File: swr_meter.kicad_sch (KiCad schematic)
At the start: 15 parts, among them U401 LTC5507, U402 LTC5507

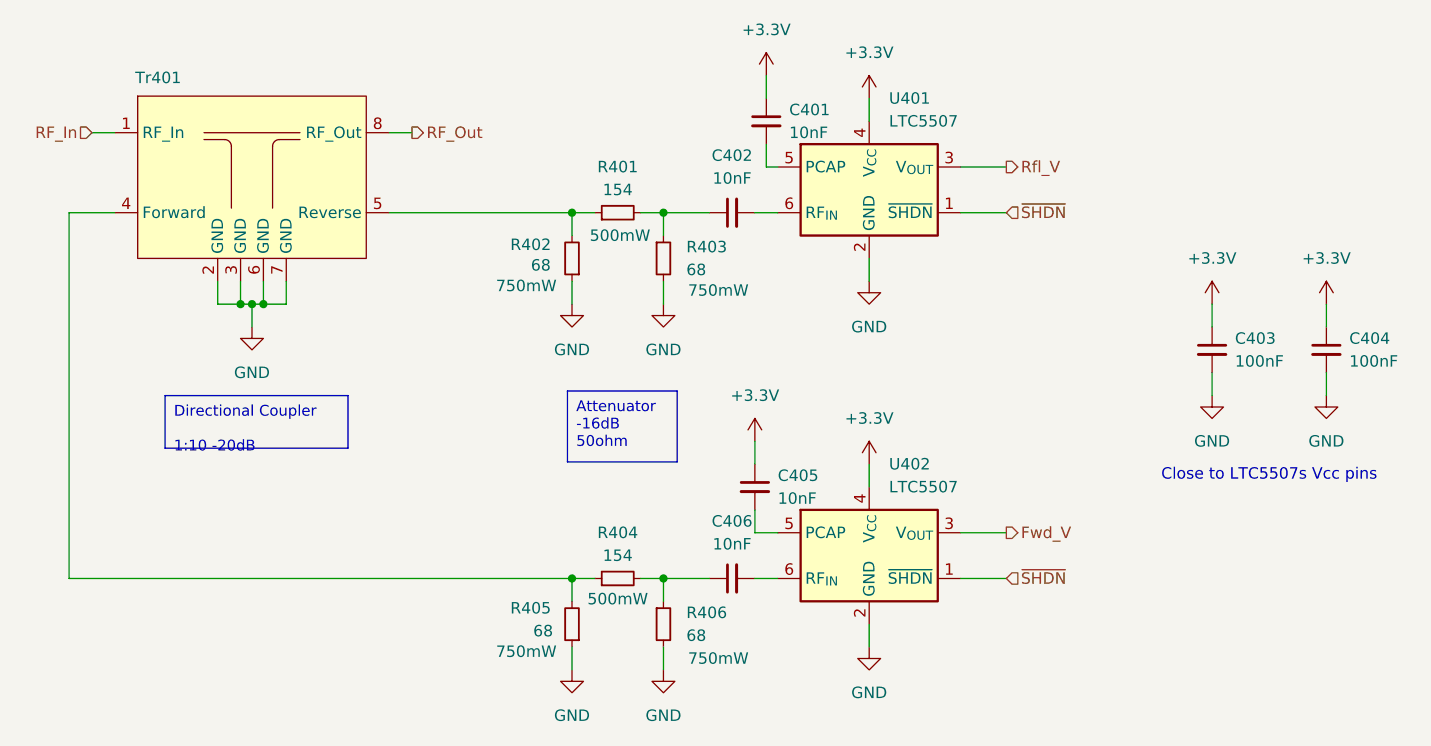
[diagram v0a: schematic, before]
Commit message: Created PDF of schematic
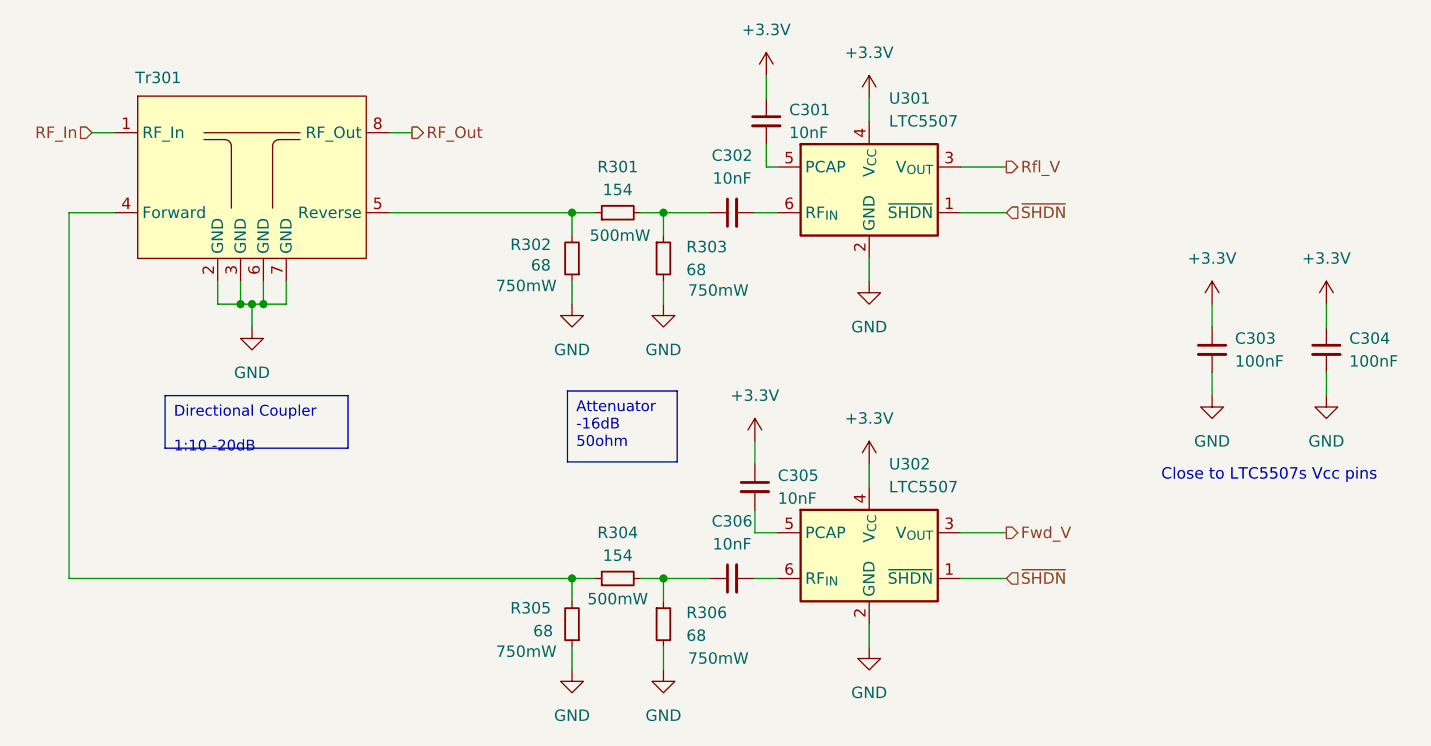
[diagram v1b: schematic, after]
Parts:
- renumbered C401 to C301, C402 to C302, C403 to C303, C404 to C304, C405 to C305, C406 to C306, R401 to R301, R402 to R302, R403 to R303, R404 to R304, R405 to R305, R406 to R306, Tr401 to Tr301, U401 to U301, U402 to U302
